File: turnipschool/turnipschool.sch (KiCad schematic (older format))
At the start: 61 parts, among them J1 USB-DEVICE-SHIELD, P1 CONN_1, P2 RESET_N, P3 DD, P4 DC, P5 3V3, P6 GND, P7 CABLE, T1 BALUN, U1 CC1111, U2 AP7313, U3 USB2412, U4 AP2511SN-7, U5 AH1806, X1 GSG-XTAL4PIN, X2 GSG-XTAL4PIN

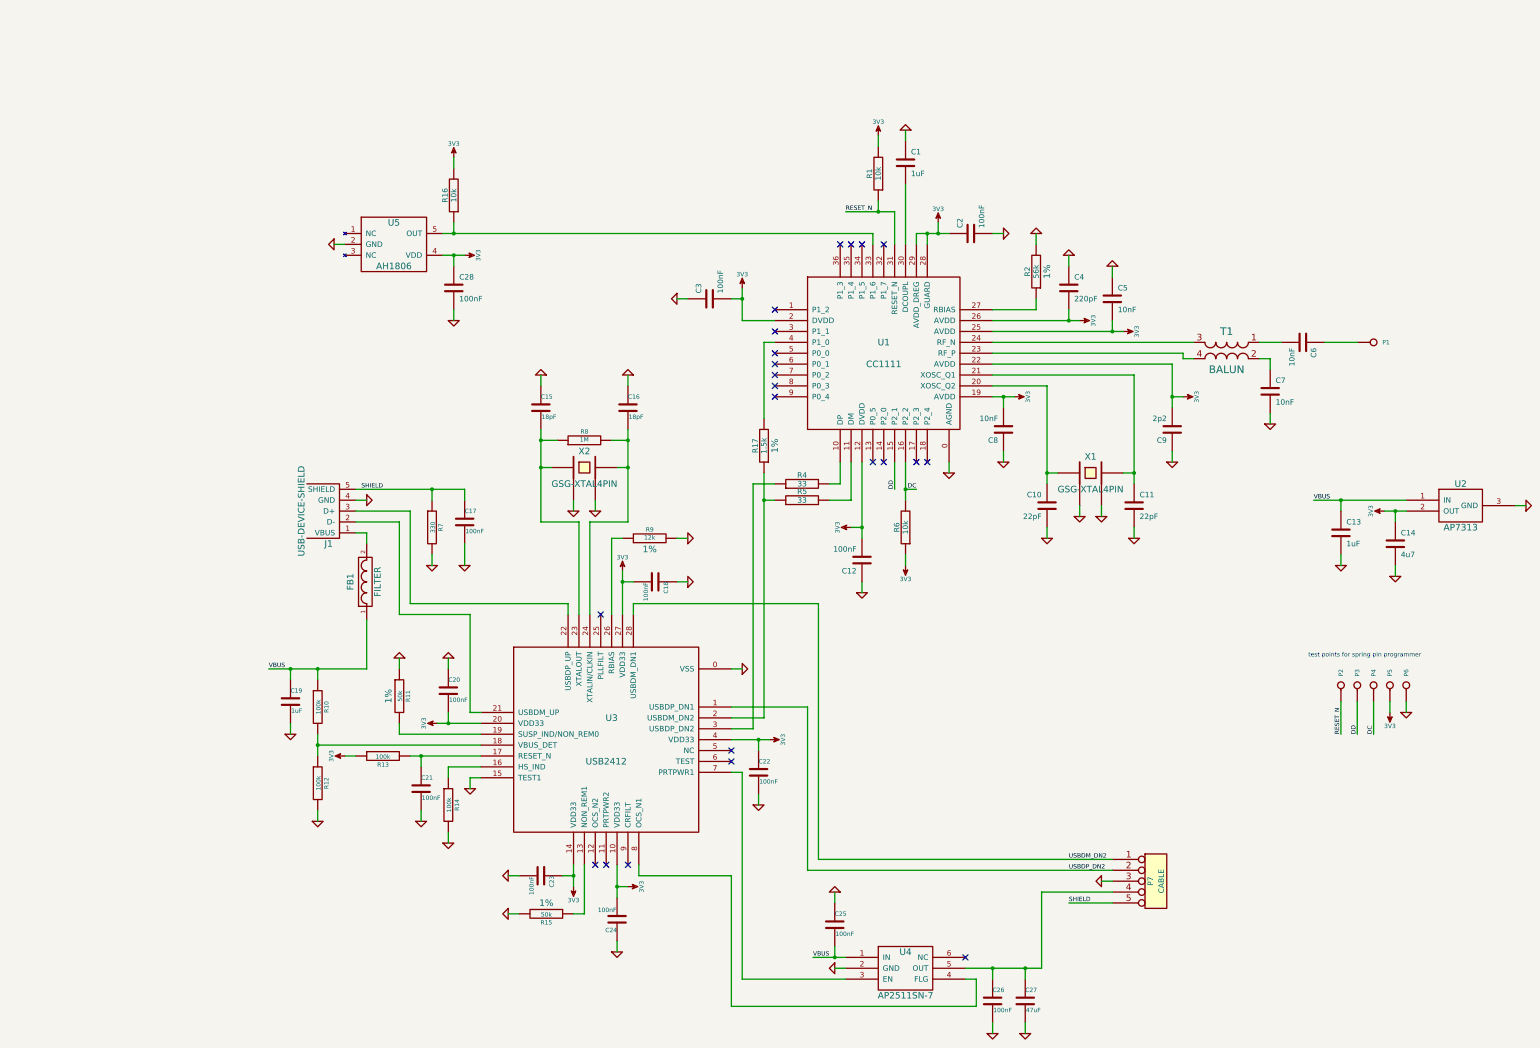
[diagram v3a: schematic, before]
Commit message: moved magnetic sensor to DC pin
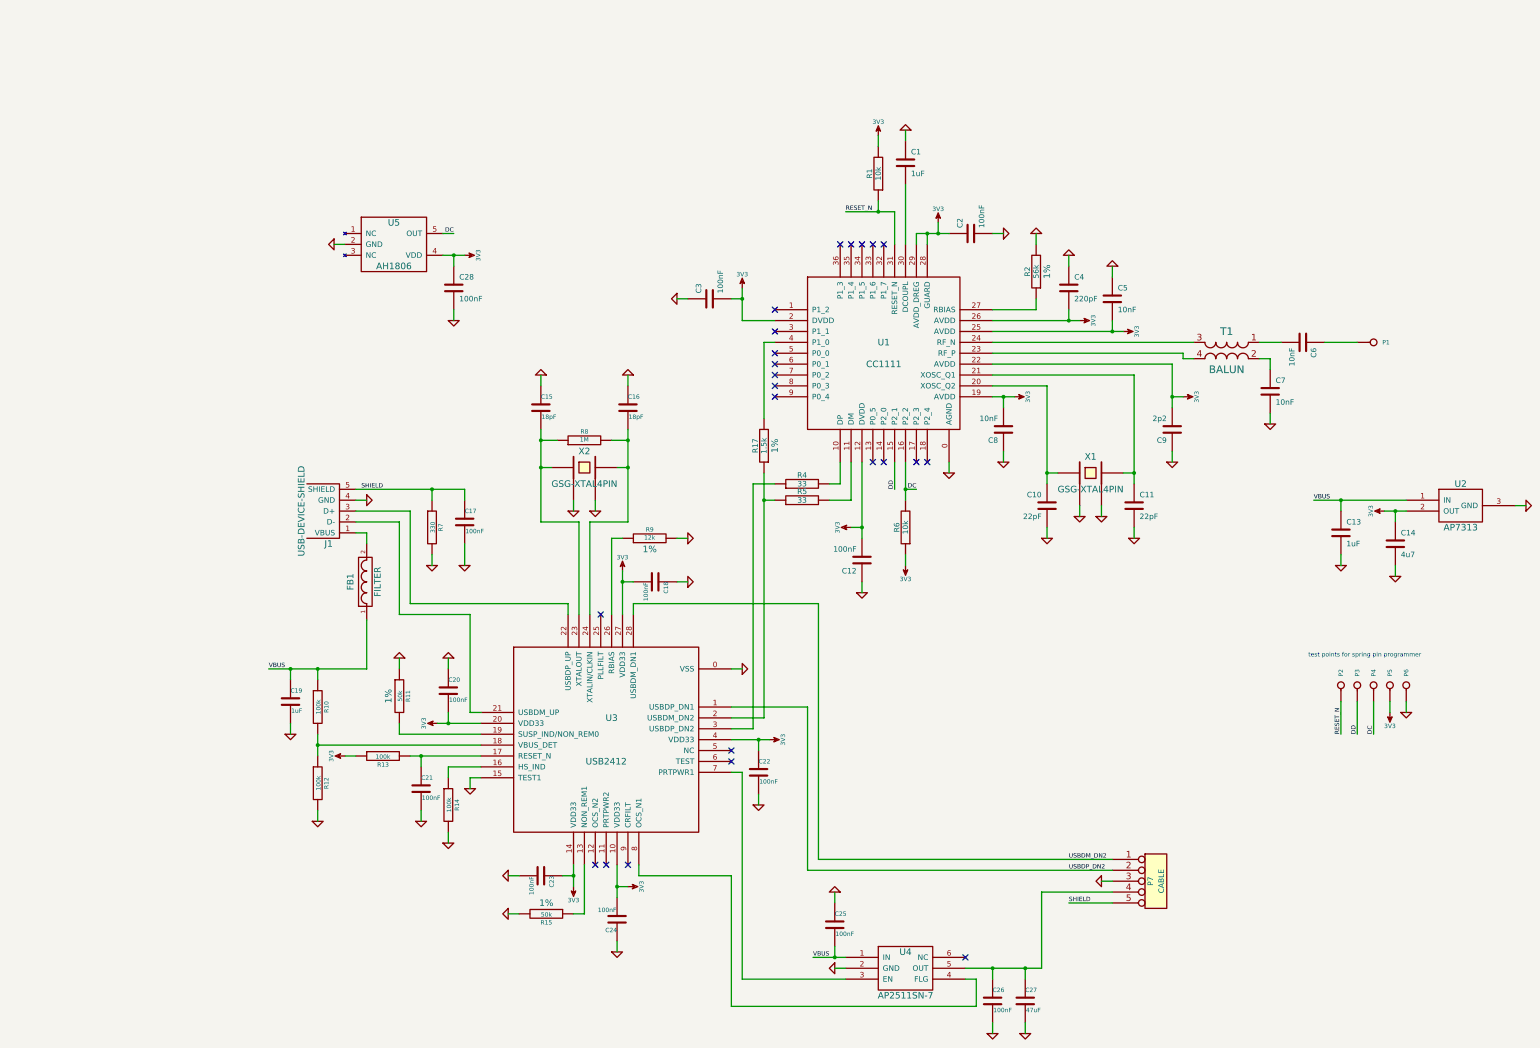
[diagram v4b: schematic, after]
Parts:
- removed R16: 10k, cc1111-legacy:GSG-0402, symbol R
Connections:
- net DC: now also U5.5 (OUT)
- net at U1.33 (P1_6): no longer U5.5 (OUT)
- no-connect marks 22 -> 23
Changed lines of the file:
@@
-$EndComp
-$Comp
-L R R16
-U 1 1 548DD7D8
-P 4750 2250
-F 0 "R16" V 4830 2250 50  0000 C CNN
-F 1 "10k" V 4750 2250 50  0000 C CNN
-F 2 "cc1111-legacy:GSG-0402" H 4750 2250 60  0001 C CNN
-F 3 "" H 4750 2250 60  0001 C CNN
-F 4 "TE Connectivity" H 4750 2250 60  0001 C CNN "Manufacturer"
-F 5 "1622826-4" H 4750 2250 60  0001 C CNN "Part Number"
-F 6 "RES 10.0K OHM 1/16W 5% 0402" H 4750 2250 60  0001 C CNN "Description"
-	1    4750 2250
-	-1   0    0    1
 $EndComp
 $Comp
@@
 $EndComp
 $Comp
-L 3V3 #PWR058
-U 1 1 548DE8FC
-P 4750 1900
-F 0 "#PWR058" H 4750 2000 40  0001 C CNN
-F 1 "3V3" H 4750 2025 40  0000 C CNN
-F 2 "" H 4750 1900 60  0001 C CNN
-F 3 "" H 4750 1900 60  0001 C CNN
-	1    4750 1900
-	1    0    0    -1
-$EndComp
-$Comp
 L 3V3 #PWR059
 U 1 1 548DEB3A
@@
 	9000 4950 8900 4950
 Wire Wire Line
-	4650 2600 8600 2600
-Wire Wire Line
-	8600 2600 8600 2700
-Connection ~ 4750 2600
-Wire Wire Line
-	4750 2600 4750 2500
-Wire Wire Line
 	4750 3400 4750 3300
 Wire Wire Line
@@
 	4750 2800 4750 2900
 Wire Wire Line
-	4650 2800 4850 2800
-Wire Wire Line
-	4750 1900 4750 2000
+	4650 2800 4750 2800
+Wire Wire Line
+	4750 2800 4850 2800
 Wire Wire Line
 	7300 6600 7400 6600
@@
 	12900 6900 12900 7200
 Wire Wire Line
-	12650 5050 13500 5050
+	12650 5050 12900 5050
+Wire Wire Line
+	12900 5050 13500 5050
 Connection ~ 8650 2400
 Wire Wire Line
-	8350 2400 8800 2400
+	8350 2400 8650 2400
+Wire Wire Line
+	8650 2400 8800 2400
 Connection ~ 12900 5050
 Wire Wire Line
@@
 Connection ~ 13400 5150
 Wire Wire Line
-	13300 5150 13500 5150
-Wire Wire Line
-	9700 3400 10500 3400
+	13300 5150 13400 5150
+Wire Wire Line
+	13400 5150 13500 5150
+Wire Wire Line
+	9700 3400 10400 3400
+Wire Wire Line
+	10400 3400 10500 3400
 Wire Wire Line
 	11350 4700 11350 4600
 Wire Wire Line
-	11350 3800 11350 4200
-Wire Wire Line
-	10200 4000 10200 4900
+	11350 3800 11350 4100
+Wire Wire Line
+	11350 4100 11350 4200
+Wire Wire Line
+	10200 4000 10200 4800
+Wire Wire Line
+	10200 4800 10200 4900
 Wire Wire Line
 	10200 4000 9700 4000
@@
 	9200 2600 9200 2500
 Wire Wire Line
-	9000 2600 9300 2600
+	9000 2600 9100 2600
+Wire Wire Line
+	9100 2600 9200 2600
+Wire Wire Line
+	9200 2600 9300 2600
 Wire Wire Line
 	9000 2600 9000 2700
@@
 	11450 3750 11550 3750
 Wire Wire Line
-	9700 4100 9900 4100
+	9700 4100 9800 4100
+Wire Wire Line
+	9800 4100 9900 4100
 Wire Wire Line
 	10300 4800 10200 4800
@@
 	8400 5300 8500 5300
 Wire Wire Line
-	8500 4700 8500 5400
+	8500 4700 8500 5300
+Wire Wire Line
+	8500 5300 8500 5400
 Connection ~ 8500 5300
 Wire Wire Line
@@
 	10800 2900 10800 3000
 Wire Wire Line
-	9700 3500 10900 3500
+	9700 3500 10800 3500
+Wire Wire Line
+	10800 3500 10900 3500
 Wire Wire Line
 	10800 3400 10800 3500
@@
 	7300 3200 7400 3200
 Wire Wire Line
-	7400 3100 7400 3400
+	7400 3100 7400 3200
+Wire Wire Line
+	7400 3200 7400 3400
 Wire Wire Line
 	7400 3400 7700 3400
@@
 	8350 9350 8250 9350
 Wire Wire Line
-	8050 9250 8350 9250
+	8050 9250 8250 9250
+Wire Wire Line
+	8250 9250 8350 9250
 Wire Wire Line
 	5000 7500 4700 7500
@@
 	4250 6600 4250 6500
 Wire Wire Line
-	4350 7400 5000 7400
+	4350 7400 4450 7400
+Wire Wire Line
+	4450 7400 5000 7400
 Wire Wire Line
 	4450 7500 4450 7400
@@
 	5000 7300 3500 7300
 Wire Wire Line
-	3500 7200 3500 7400
+	3500 7200 3500 7300
+Wire Wire Line
+	3500 7300 3500 7400
 Connection ~ 3500 7300
 Wire Wire Line
@@
 	5550 4000 5550 3900
 Wire Wire Line
-	9450 9350 10150 9350
+	9450 9350 9700 9350
+Wire Wire Line
+	9700 9350 10000 9350
+Wire Wire Line
+	10000 9350 10150 9350
 Wire Wire Line
 	12750 3600 13050 3600
 Wire Wire Line
-	8900 4700 8900 5050
+	8900 4700 8900 4950
+Wire Wire Line
+	8900 4950 8900 5050
 Wire Wire Line
 	13350 6900 13350 7000
 Wire Wire Line
-	3850 4950 4850 4950
+	3850 4950 4550 4950
+Wire Wire Line
+	4550 4950 4850 4950
 Wire Wire Line
 	3950 5050 3850 5050
@@
 Connection ~ 8250 9250
 Wire Wire Line
-	4600 7100 5000 7100
-Wire Wire Line
-	6300 5700 6300 6100
-Wire Wire Line
-	6250 8400 6250 8700
+	4600 7100 4700 7100
+Wire Wire Line
+	4700 7100 5000 7100
+Wire Wire Line
+	6300 5700 6300 5800
+Wire Wire Line
+	6300 5800 6300 6100
+Wire Wire Line
+	6250 8400 6250 8600
+Wire Wire Line
+	6250 8600 6250 8700
 Connection ~ 9700 9350
 Wire Wire Line
@@
 	10000 9350 10000 9450
 Wire Wire Line
-	11000 3900 11000 4900
+	11000 3900 11000 4800
+Wire Wire Line
+	11000 4800 11000 4900
 Wire Wire Line
 	11000 3900 9700 3900
@@
 	10700 8550 10800 8550
 Wire Wire Line
-	6350 4400 6350 5250
+	6350 4400 6350 4500
+Wire Wire Line
+	6350 4500 6350 4750
+Wire Wire Line
+	6350 4750 6350 5250
 Wire Wire Line
 	6350 5250 6000 5250
@@
 	6000 5250 6000 6100
 Wire Wire Line
-	5550 4400 5550 5250
+	5550 4400 5550 4500
+Wire Wire Line
+	5550 4500 5550 4750
+Wire Wire Line
+	5550 4750 5550 5250
 Wire Wire Line
 	5550 5250 5900 5250
@@
 	3250 6700 3250 6600
 Wire Wire Line
-	3050 6600 3950 6600
+	3050 6600 3250 6600
+Wire Wire Line
+	3250 6600 3500 6600
+Wire Wire Line
+	3500 6600 3950 6600
 Wire Wire Line
 	3500 6600 3500 6700
@@
 	7550 7750 7550 7850
 Wire Wire Line
-	7300 7250 7650 7250
+	7300 7250 7550 7250
+Wire Wire Line
+	7550 7250 7650 7250
 Wire Wire Line
 	7550 7250 7550 7350
@@
 $EndComp
 Wire Wire Line
-	5850 8400 5850 8600
+	5850 8400 5850 8500
+Wire Wire Line
+	5850 8500 5850 8600
 Wire Wire Line
 	5850 8500 5750 8500
@@
 NoConn ~ 7700 3500
 Wire Wire Line
-	7600 4800 7600 7050
+	7600 4800 7600 5050
+Wire Wire Line
+	7600 5050 7600 7050
 Wire Wire Line
 	7600 7050 7300 7050
@@
 Wire Wire Line
 	6250 9100 6250 9200
+Wire Wire Line
+	4750 2600 4650 2600
+Text Label 4750 2600 2    40   ~ 0
+DC
+NoConn ~ 8600 2700
 $EndSCHEMATC
